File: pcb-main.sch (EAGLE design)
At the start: 90 parts, among them U1 SHHN000A3CL41Z, U2 F15S48

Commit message: Update
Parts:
- removed C21: 10u/50V, capacitors-electrolytic:C-E2-5
- removed DA1: LM317, regulators-linear:LM317
- removed DA2: LM337, regulators-linear:LM337
- removed R4: 1k, resistors:R-0207/10
- removed R5, R6: 412R, resistors:R-0207/10
- removed S1, S2: (no value), switches:JUMPER-1POS-SOLDER
- removed VD2, VD3, VD6, VD7: 1N4004GP, diodes:1N4004GP
- removed VD4, VD5: LM329, diodes-zener:LM329
- added L2: BL01RN1A1F1J, inductors:BL01RN1A1F1J
- added U4: (no value), module-footprints:F-DUAL-SUPPLY
- C1: value 10u/50V -> 10u/35V
- C2: value 100u/25V -> 10u/35V; device capacitors-electrolytic:C-E2,5-7 -> capacitors-electrolytic:C-E2-5
- C20: value 100u/25V -> 100u/63V; device capacitors-electrolytic:C-E2,5-7 -> capacitors-electrolytic:C-E5-10
- C3: value 100u/25V -> 33u/25V; device capacitors-electrolytic:C-E2,5-7 -> capacitors-electrolytic:C-E2-5
- C4, C5: value 100n -> 100u/25V; device capacitors:C-050-025X075 -> capacitors-electrolytic:C-E2,5-7
- C6: value 47u/35V -> 100n; device capacitors-electrolytic:C-E2-5 -> capacitors:C-050-024X44
- C7, C9: value 47u/35V -> 100u/25V; device capacitors-electrolytic:C-E2-5 -> capacitors-electrolytic:C-E2,5-7
- C8: value 47u/35V -> 100u/63V; device capacitors-electrolytic:C-E2-5 -> capacitors-electrolytic:C-E5-10
- R1, R2: value 1.5k -> 2.2R
- R11, R12: value 6.81k -> 6.81k*
- R3: value 1k -> 2.2R
- U1: value SHHN000A3CL41Z -> IH1224SH; device regulators-switch-mode:SHHN000A3CL41Z -> regulators-switch-mode:IH1224SH
- U2: value F15S48 -> RS3-1215D; device regulators-switch-mode:F15S48 -> regulators-switch-mode:RS3-1215D
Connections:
- removed net N$20: S1.1, U1.EN
- removed net N$3 (its old number): C21.+, L1.1, VD12.C
- new net N$7: R1.1, U1.V+
- net +12V: now also C7.+, U4.P+12V; no longer C8.+, DA1.OUT, R1.2, R3.2, VD2.A, VD7.C
- net +15V: now also C4.+, R2.2, U4.P+VA; no longer C2.+, C4.2, DA1.IN, S2.2, U1.V+, U2.IN, VD2.C
- net +48V: now also C8.+, R1.2; no longer S2.1, U2.OUT
- net -12V: now also U4.P-12V; no longer DA2.OUT, R2.1, R4.1, VD3.C, VD6.A
- net -15V: now also C5.-, R3.2, U4.P-VA; no longer C3.-, C5.1, DA2.IN, U1.V-, VD3.A
- net CHASSIS: now also C2.-, C3.-, C6.1, U2.IN-; no longer C21.-, S1.2
- net GND: now also C4.-, C5.+, U1.V-, U4.GND, U4.GND1; no longer C2.-, C3.+, C4.1, C5.2, C6.+, R5.2, R6.1, U1.GND
- net N$1: now also C2.+, L2.2, U2.IN+; no longer C7.+, DA1.GND, R1.1, VD5.C, VD7.A
- net N$5: now also C3.+, C6.2, L1.1, L2.1, VD12.C; no longer R3.1, R6.2, VD5.A
- net N$8: now also R2.1, U2.V+; no longer C6.-, DA2.GND, R2.2, VD4.A, VD6.C
- net N$9: now also R3.1, U2.V-; no longer R4.2, R5.1, VD4.C
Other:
- note removed: "R = Vout/(9.08*10^-3)-908R"
- moved on the sheet: C1, C2, C22, C23, C3, C41, C42, C7, C8, C9, DA3.2, DA6*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

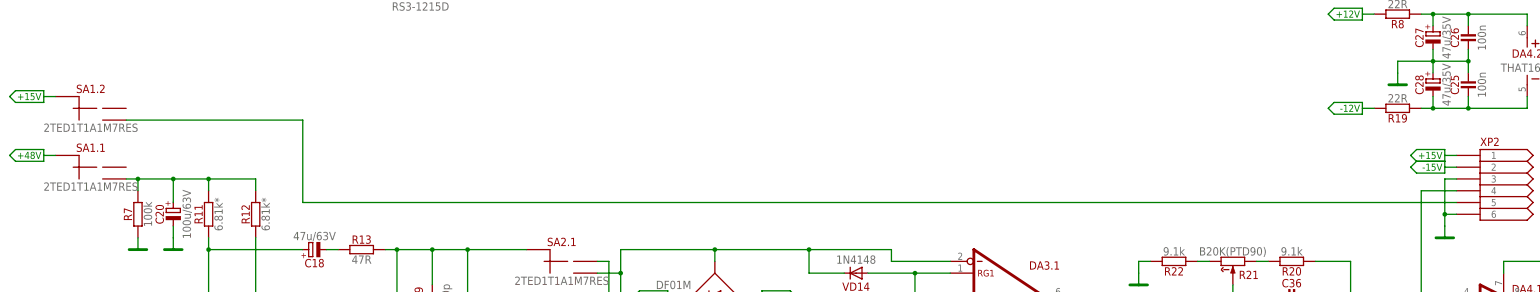
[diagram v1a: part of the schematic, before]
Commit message: Switch footprint fix
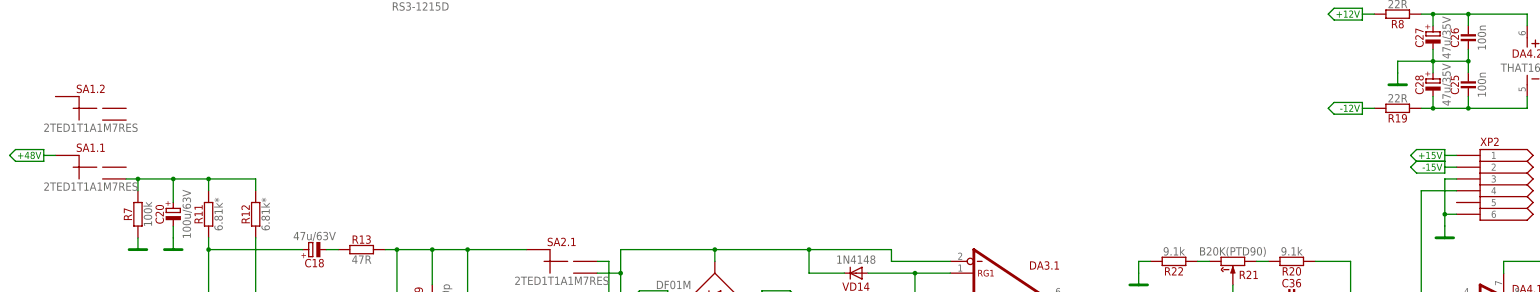
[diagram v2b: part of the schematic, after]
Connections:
- removed net N$42: SA1.2.2, XP2.5
- net +15V: no longer SA1.2.CM
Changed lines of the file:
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@@
 <part name="SA2" library="switches" deviceset="2TED1T1A1M7RES" device=""/>
 <part name="PWR18" library="supply" deviceset="+48V" device=""/>
-<part name="PWR11" library="supply" deviceset="+15V" device=""/>
 <part name="PWR19" library="supply" deviceset="+15V" device=""/>
 <part name="PWR20" library="supply" deviceset="-15V" device=""/>
@@
 <instance part="DA6" gate="*" x="243.84" y="15.24"/>
 <instance part="PWR18" gate="G$1" x="-63.5" y="-33.02" rot="R90"/>
-<instance part="PWR11" gate="G$1" x="-63.5" y="-20.32" rot="R90"/>
 <instance part="PWR19" gate="G$1" x="238.76" y="-33.02" rot="R90"/>
 <instance part="PWR20" gate="G$1" x="238.76" y="-35.56" rot="R90"/>
@@
 <net name="+15V" class="0">
 <segment>
-<pinref part="SA1" gate=".2" pin="CM"/>
-<wire x1="-63.5" y1="-20.32" x2="-60.96" y2="-20.32" width="0.1524" layer="91"/>
-<pinref part="PWR11" gate="G$1" pin="+15V"/>
-</segment>
-<segment>
 <pinref part="PWR19" gate="G$1" pin="+15V"/>
 <pinref part="XP2" gate="G$1" pin="1"/>
@@
 </segment>
 </net>
-<net name="N$42" class="0">
-<segment>
-<wire x1="241.3" y1="-43.18" x2="-7.62" y2="-43.18" width="0.1524" layer="91"/>
-<wire x1="-7.62" y1="-43.18" x2="-7.62" y2="-25.4" width="0.1524" layer="91"/>
-<pinref part="SA1" gate=".2" pin="2"/>
-<wire x1="-7.62" y1="-25.4" x2="-45.72" y2="-25.4" width="0.1524" layer="91"/>
-<pinref part="XP2" gate="G$1" pin="5"/>
-</segment>
-</net>

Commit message: Main Board
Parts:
- added PCB1: R-PREAMP rev.A, module-footprints:GENERIC-LOGO
- C1, C2: value 10u/35V -> 10U/35V(11MM); device capacitors-electrolytic:C-E2-5 -> capacitors-electrolytic:10U/35V(11MM)
- C10, C35: value 47p -> 47P(TH); device capacitors:C-050-024X44 -> capacitors:47P(TH)
- C11, C12, C19, C33, C34: value 470p -> 470P(FILM); device capacitors:C-050-055X075 -> capacitors:470P(FILM)
- C13, C14, C29, C30: value 47u/35V -> 47U/35V(NP); device capacitors-electrolytic:C_BIPOLAR-E5-10 -> capacitors-electrolytic:47U/35V(NP)
- C15, C16: value 100p -> 100P(FILM); device capacitors:C-050-045X075 -> capacitors:100P(FILM)
- C17, C18: value 47u/63V -> 47U/63V; device capacitors-electrolytic:C-E5-10 -> capacitors-electrolytic:47U/63V
- C20, C8: value 100u/63V -> 100U/63V; device capacitors-electrolytic:C-E5-10 -> capacitors-electrolytic:100U/63V
- C22, C23, C25, C26, C41, C42, C6: value 100n -> 100N(TH); device capacitors:C-050-024X44 -> capacitors:100N(TH)
- C24, C43: value 3300u/6.3V -> 3300U/6V3; device capacitors-electrolytic:C-E5-10 -> capacitors-electrolytic:3300U/6V3
- C27, C28: value 47u/35V -> 47U/35V; device capacitors-electrolytic:C-E2-5 -> capacitors-electrolytic:47U/35V
- C3: value 33u/25V -> 47U/35V; device capacitors-electrolytic:C-E2-5 -> capacitors-electrolytic:47U/35V
- C31, C32: value 330n -> 330N(FILM); device capacitors:C-050-035X075 -> capacitors:330N(FILM)
- C36: value 22p -> 22P(TH); device capacitors:C-050-024X44 -> capacitors:22P(TH)
- C4, C5, C7, C9: value 100u/25V -> 100U/25V; device capacitors-electrolytic:C-E2,5-7 -> capacitors-electrolytic:100U/25V
- R1, R2, R3: value 2.2R -> 2R2(TH); device resistors:R-0207/10 -> resistors:2R2(TH)
- R10, R9: value 4.99k -> 4K99*(TH); device resistors:R-0207/10 -> resistors:4K99*(TH)
- R11, R12: value 6.81k* -> 6K81*(TH); device resistors:R-0207/10 -> resistors:6K81*(TH)
- R13, R14: value 47R -> 47R(TH); device resistors:R-0207/10 -> resistors:47R(TH)
- R15, R16: value 1.21k -> 1K21*(TH); device resistors:R-0207/10 -> resistors:1K21*(TH)
- R18: value 5R -> 5R(TH); device resistors:R-0207/10 -> resistors:5R(TH)
- R19, R8: value 22R -> 20R(TH); device resistors:R-0207/10 -> resistors:20R(TH)
- R20, R22: value 9.1k -> 9K1(TH); device resistors:R-0207/10 -> resistors:9K1(TH)
- R23: value 1k -> 1K(TH); device resistors:R-0207/10 -> resistors:1K(TH)
- R7: value 100k -> 100K(TH); device resistors:R-0207/10 -> resistors:100K(TH)
- U1: value IH1224SH -> IH1224DH; device regulators-switch-mode:IH1224SH -> regulators-switch-mode:IH1224DH
- U3: value (none) -> 56DP30-GAIN
- XS4: value PJ-051AH -> 712RA; device connectors:PJ-051AH -> connectors:712RA

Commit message: Add component value for LT3032-12 module
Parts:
- U4: value (none) -> F-LT3032-12
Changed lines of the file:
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@@
 <part name="PWR2" library="supply" deviceset="+15V" device=""/>
 <part name="PWR3" library="supply" deviceset="-15V" device=""/>
-<part name="U4" library="module-footprints" deviceset="F-DUAL-SUPPLY" device=""/>
+<part name="U4" library="module-footprints" deviceset="F-DUAL-SUPPLY" device="" value="F-LT3032-12"/>
 <part name="PWR4" library="supply" deviceset="+15V" device=""/>
 <part name="PWR5" library="supply" deviceset="-15V" device=""/>

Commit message: Change DC Connector
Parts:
- XS4: value 712RA -> 722RA; device connectors:712RA -> connectors:722RA
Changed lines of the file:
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@@
 </classes>
 <parts>
-<part name="XS4" library="connectors" deviceset="712RA" device=""/>
+<part name="XS4" library="connectors" deviceset="722RA" device=""/>
 <part name="XS1" library="connectors" deviceset="NCJ6FAH-0" device=""/>
 <part name="C10" library="capacitors" deviceset="?" device="47P(TH)" value="47P(TH)"/>

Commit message: Change 20R -> 22R
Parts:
- R19, R8: value 20R(TH) -> 22R(TH); device resistors:20R(TH) -> resistors:22R(TH)
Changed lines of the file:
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@@
 <part name="C27" library="capacitors-electrolytic" deviceset="?" device="47U/35V" value="47U/35V"/>
 <part name="C28" library="capacitors-electrolytic" deviceset="?" device="47U/35V" value="47U/35V"/>
-<part name="R8" library="resistors" deviceset="?" device="20R(TH)" value="20R(TH)"/>
-<part name="R19" library="resistors" deviceset="?" device="20R(TH)" value="20R(TH)"/>
+<part name="R8" library="resistors" deviceset="?" device="22R(TH)" value="22R(TH)"/>
+<part name="R19" library="resistors" deviceset="?" device="22R(TH)" value="22R(TH)"/>
 <part name="PWR12" library="supply" deviceset="+12V" device=""/>
 <part name="PWR13" library="supply" deviceset="-12V" device=""/>
